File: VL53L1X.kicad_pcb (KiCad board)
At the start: 2 copper layers, 9.8 x 6.6 mm, 4 parts, among them IC1 VL53L1X, J1 Conn_01x06

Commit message: Specify JLCPCB order number location
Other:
- board text added: "JLCJLCJLCJLC"
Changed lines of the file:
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@@
     (effects (font (size 0.8 0.8) (thickness 0.153)))
+  )
+  (gr_text "JLCJLCJLCJLC" (at 152.4 88.1) (layer "B.SilkS")
+    (effects (font (size 0.8 0.7) (thickness 0.15)) (justify mirror))
   )
   (gr_text "RX\n\nTX\n" (at 152.4 86.2 270) (layer "F.SilkS")

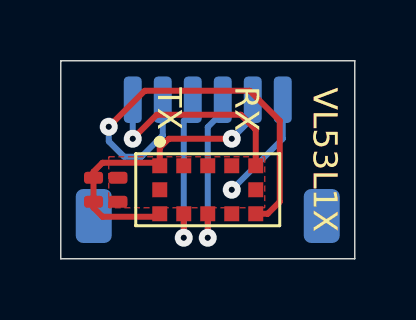
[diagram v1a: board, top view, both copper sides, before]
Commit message: Switch from 0201/0603Metric to 0402 caps
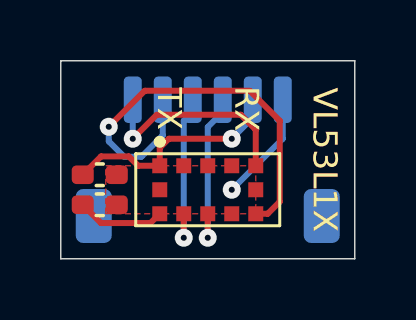
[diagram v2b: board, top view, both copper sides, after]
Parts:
- C1, C2: footprint Capacitor_SMD:C_0201_0603Metric_Pad0.64x0.40mm_HandSolder -> Capacitor_SMD:C_0402_1005Metric_Pad0.74x0.62mm_HandSolder
- moved C1 0.22 mm to (148.8, 89.4)
- moved C2 0.22 mm to (148.8, 88.4)
